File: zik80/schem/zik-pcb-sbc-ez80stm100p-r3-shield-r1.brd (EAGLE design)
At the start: 149.8 x 100 mm, 45 parts, among them IC1 TPS7133QP, U2 FT232RLSSOP

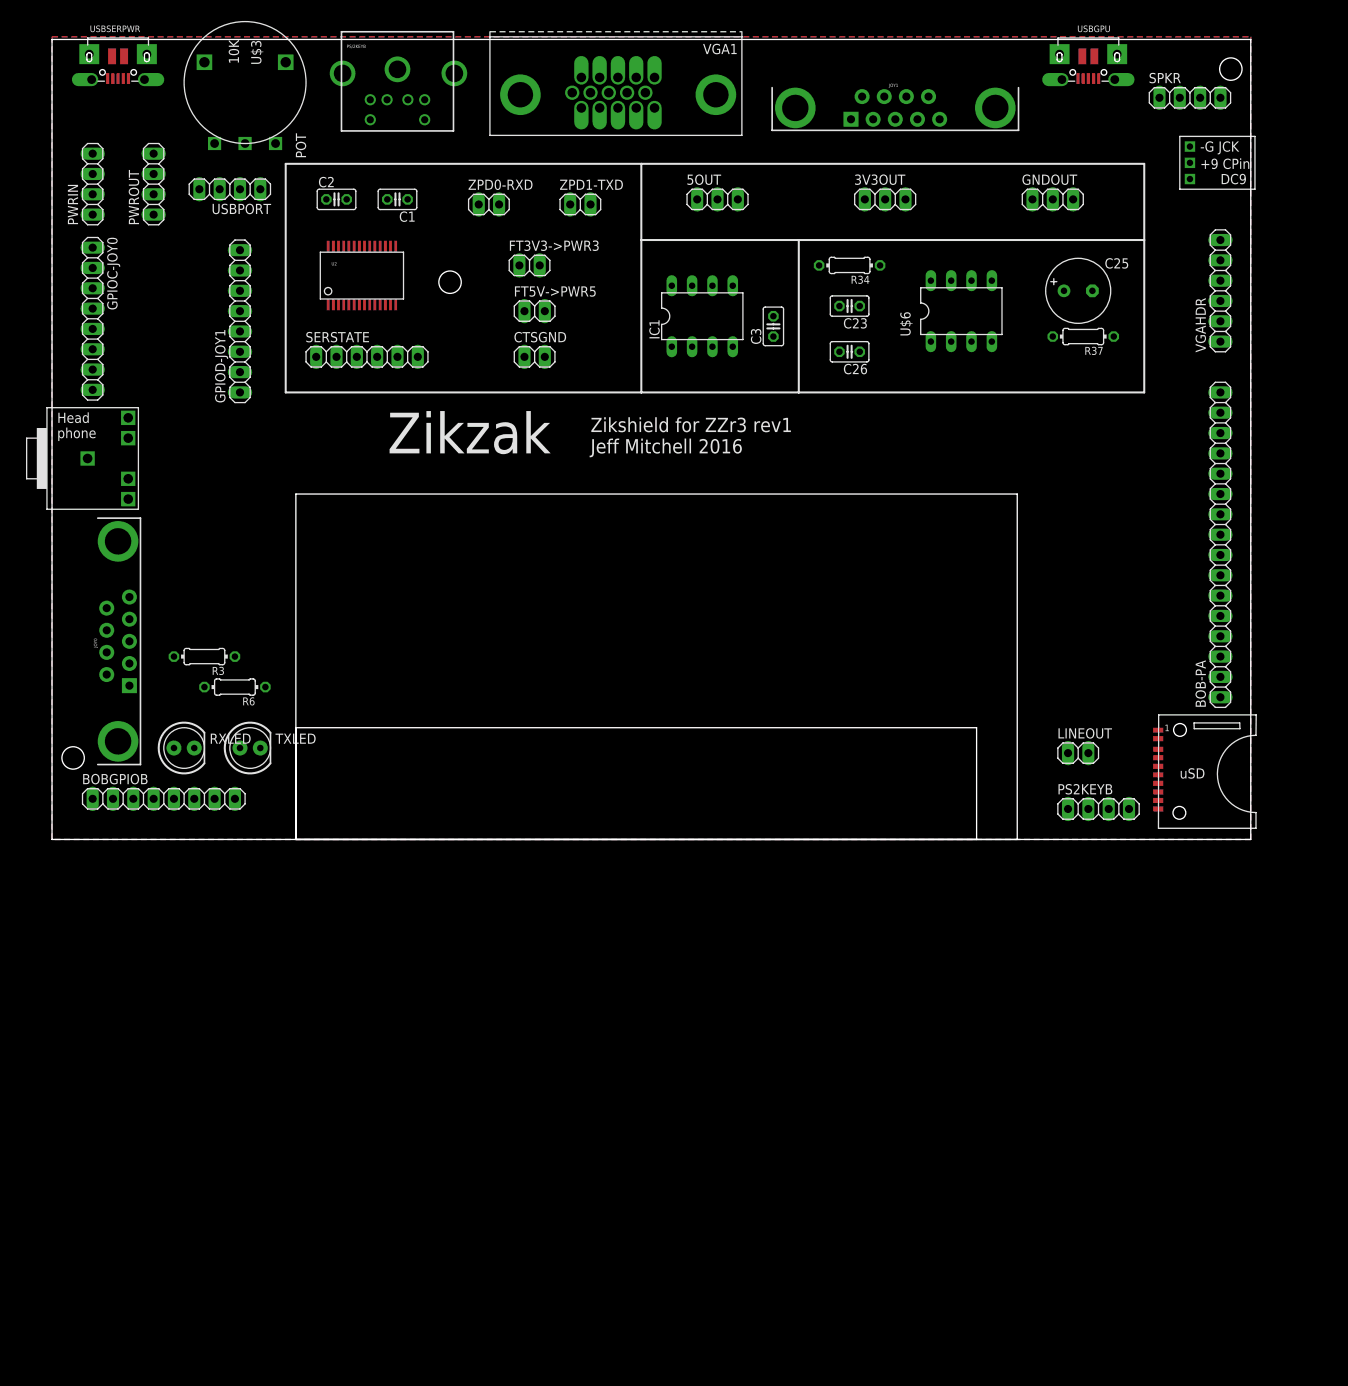
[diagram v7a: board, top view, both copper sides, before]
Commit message: Shield schem nearly final, just need to lay down traces on pcb
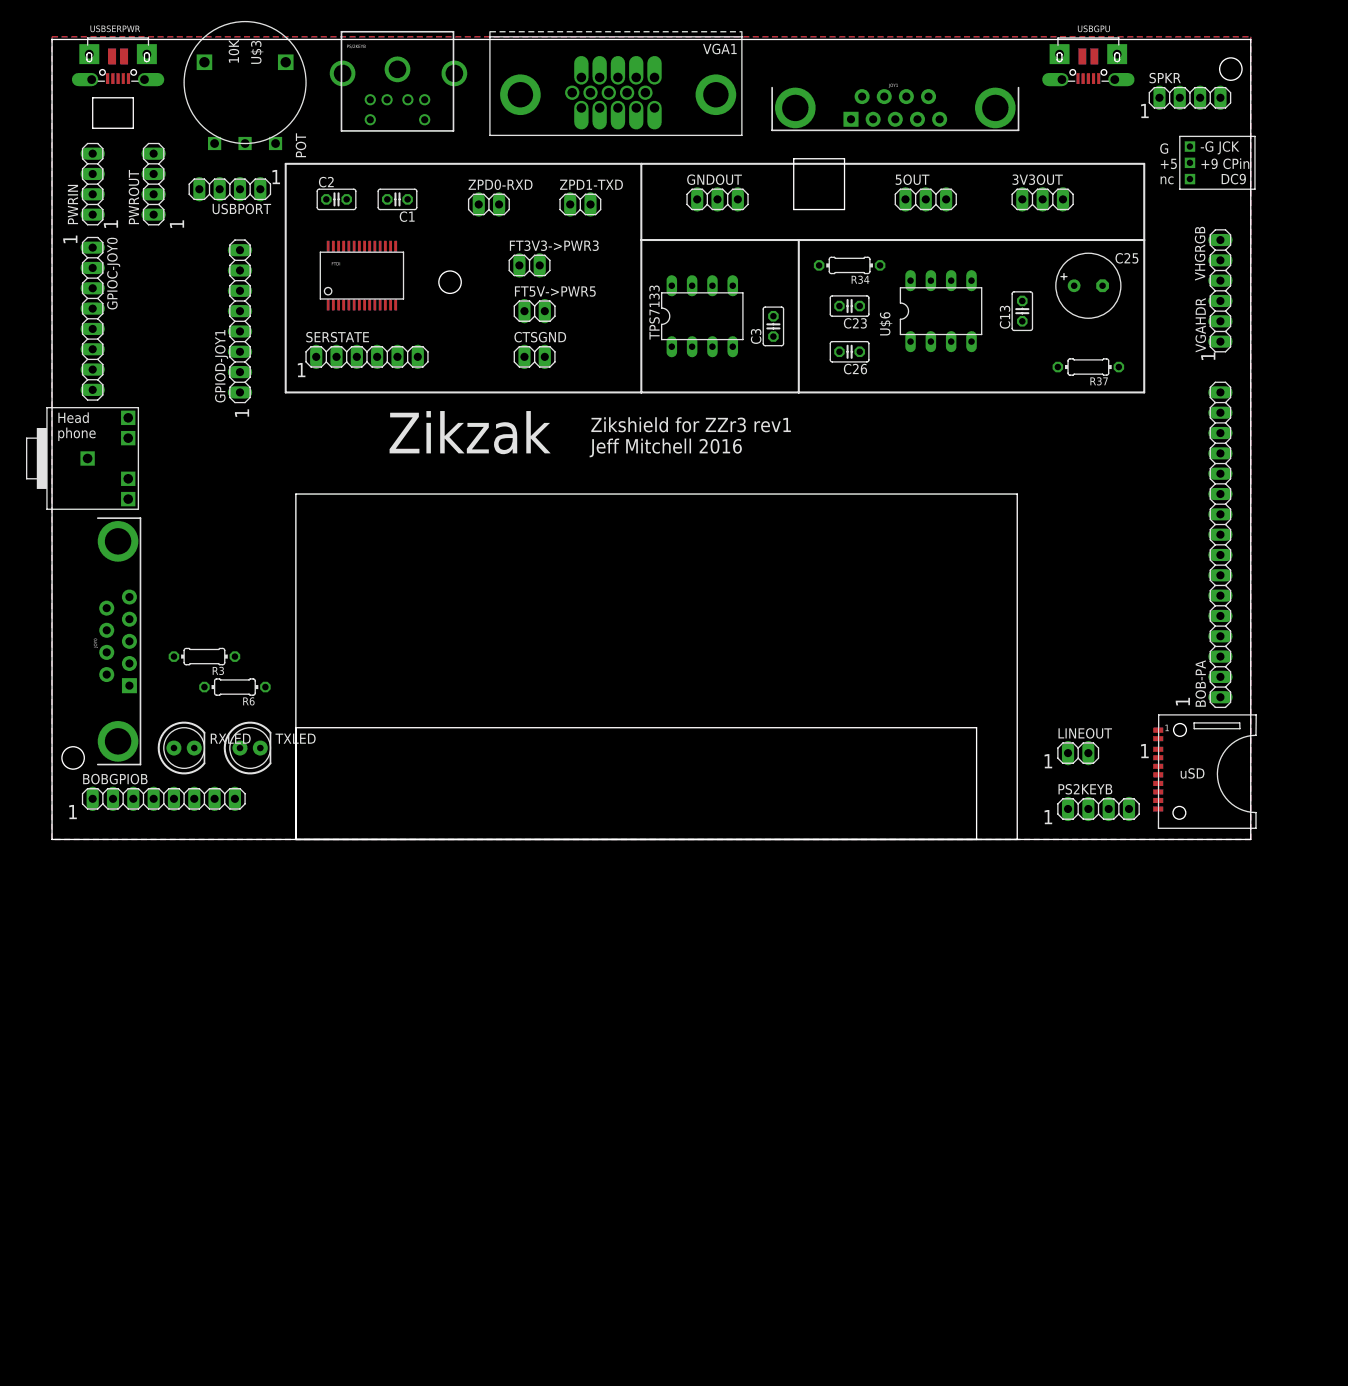
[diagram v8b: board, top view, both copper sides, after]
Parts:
- added C13: .1uF, rcl:C025-025X050
- moved GNDOUT 41.9 mm to (83.2, 80.0)
- moved 5OUT 26.0 mm to (109.2, 80.0)
- moved 3V3OUT 19.7 mm to (123.8, 80.0)
- moved R37 3.86 mm to (129.5, 59.1)
- moved U$6 2.54 mm to (107.3, 63.5)
- moved C25 1.42 mm to (129.5, 69.2)
- renumbered IC1 to TPS7133, U$5 to HEADPHONE, U2 to FTDI
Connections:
- removed net +5V: U$6.6, VGA1.9
- removed net N$26: VGAHDR.1
- removed net N$27: VGAHDR.2
- removed net N$28: VGAHDR.3
- removed net N$29: VGAHDR.4
- removed net N$30: VGAHDR.5
- removed net N$31: VGAHDR.6
- new net SB: VGA1.3, VGAHDR.6
- new net SG: VGA1.2, VGAHDR.5
- new net SH: VGA1.13, VGAHDR.2
- new net SR: VGA1.1, VGAHDR.4
- new net SV: VGA1.14, VGAHDR.1
- net GND: now also C13.2, SPKR.4, VGA1.10, VGA1.5, VGA1.6, VGA1.7, VGA1.8, VGAHDR.3
- net PWR5: now also C13.1, U$6.6, VGA1.9
- net SPA10: now also USBGPU.ID
- net SPA11: now also USBGPU.D-; no longer USBGPU.D+
- net SPA12: now also USBGPU.D+; no longer USBGPU.D-
- net USB_D+: now also USBSERPWR.D+; no longer USBSERPWR.D-
- net USB_D-: now also USBSERPWR.D-; no longer USBSERPWR.D+
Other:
- outline, holes or cut-outs redrawn
- board text added: "1"
- board text added: "G +5 nc"
- board text added: "VHGRGB"
